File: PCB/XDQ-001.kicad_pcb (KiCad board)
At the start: 4 copper layers, 45 x 50 mm, 66 parts, among them J1 RADIO, J2 ESC, J3 GPS, J4 SWD, J5 USB_B_Micro, J6 BEC CONECTOR, U1 USBLC6-2P6, U2 AP2112K-3.3, U3 STM32F411CEUx, U4 AP2112K-3.3, U5 W25Q32JVSS, U6 AP2112K-3.3, U7 ICM-42688-P, U8 BMP280, U9 MMC5983MA, Y1 8Mhz

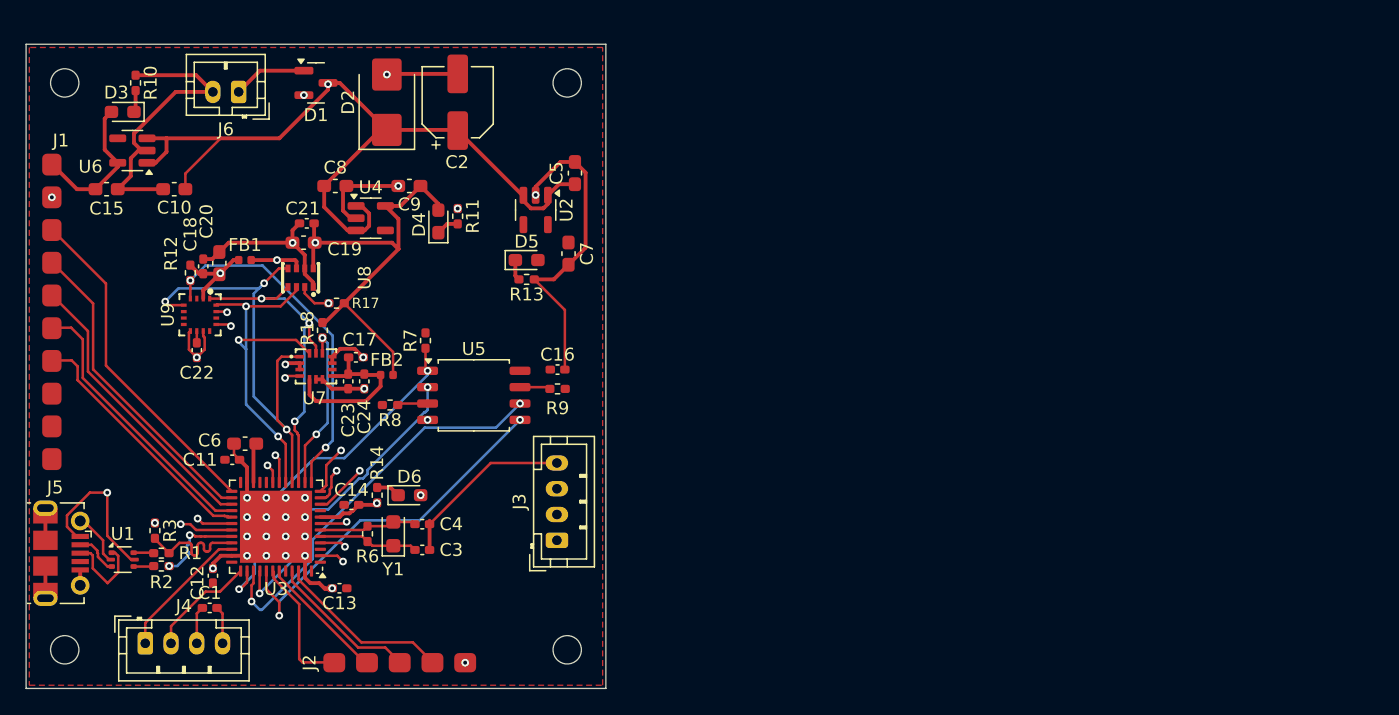
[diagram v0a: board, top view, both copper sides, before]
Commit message: Updated FCB and documentation
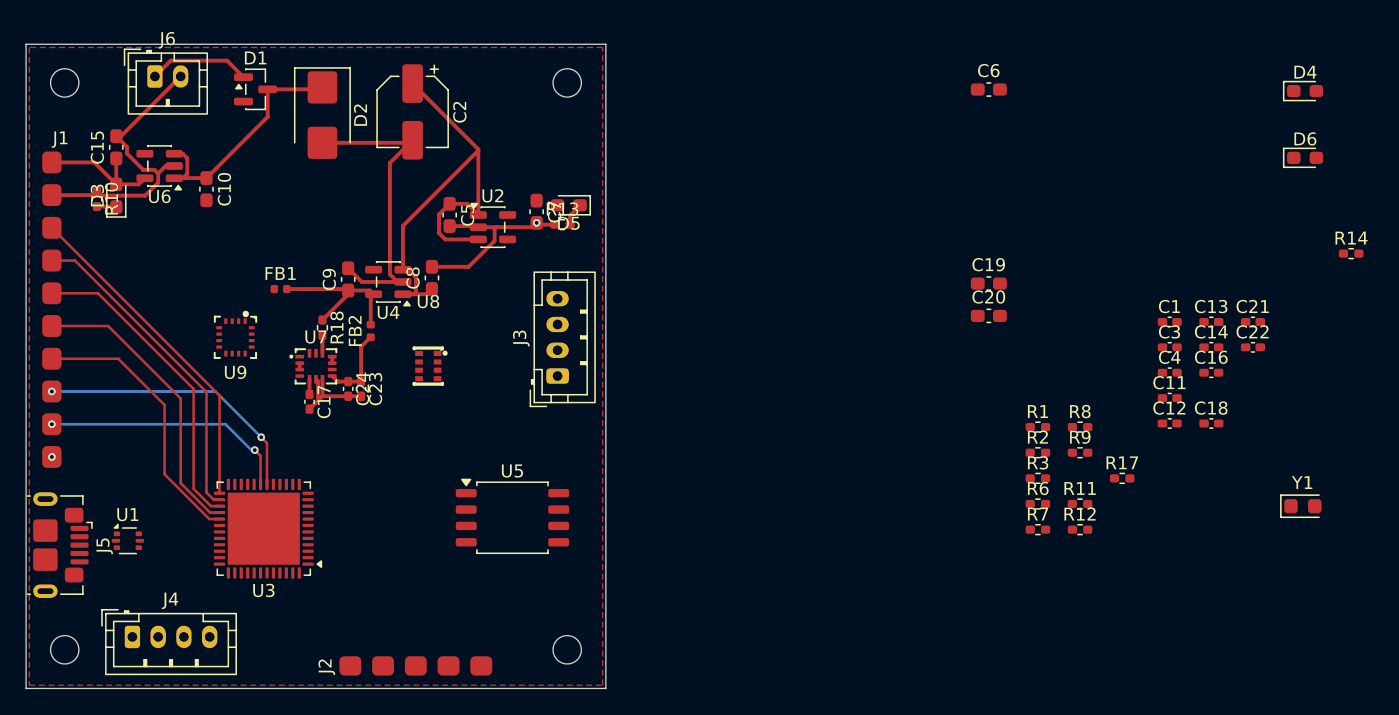
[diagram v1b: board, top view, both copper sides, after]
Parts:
- J5: footprint Connector_USB:USB_Micro-B_Molex-105017-0001 -> huellas_simplificadas:USB_Micro-B_GCT_USB3076-30-A
- moved C22 82.0 mm to (184.2, 97.5), turned to 0 degrees
- moved C18 79.2 mm to (181.0, 103.4), turned to 0 degrees
- moved R14 77.9 mm to (191.8, 90.2), turned to 0 degrees
- moved C1 77.8 mm to (177.8, 95.6)
- moved C12 75.2 mm to (177.8, 103.4), turned to 0 degrees
- moved D6 74.3 mm to (188.3, 82.8)
- moved C21 73.8 mm to (184.2, 95.6), turned to 0 degrees
- moved C11 72.9 mm to (177.8, 101.5)
- moved R12 71.9 mm to (170.8, 111.7), turned to 0 degrees
- moved C13 70.8 mm to (181.0, 95.6), turned to 0 degrees
- moved Y1 70.6 mm to (188.1, 109.9), turned to 0 degrees
- moved R1 68.7 mm to (167.5, 103.7), turned to 0 degrees
- moved R3 68.7 mm to (167.5, 107.7), turned to 0 degrees
- moved R2 68.6 mm to (167.5, 105.7), turned to 0 degrees
- moved D4 68.0 mm to (188.3, 77.6), turned to 0 degrees
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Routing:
- net GND: track 142.3 -> 70.6 mm, vias 31 -> 1
- net /VBUS: track 49.5 -> 0.00 mm, vias 2 -> 0
- net /GPS_TX: track 37.2 -> 0.00 mm, vias 1 -> 0
- net /IMU_MISO: track 36.7 -> 0.00 mm, vias 3 -> 0
- net /GPS_RX: track 34.9 -> 0.00 mm, vias 1 -> 0
- net /FLASH_SCK: track 31.0 -> 0.00 mm, vias 2 -> 0
- net +3V3_ANALOG: track 42.9 -> 12.5 mm, vias 2 -> 0
- net /FLASH_MOSI: track 29.5 -> 0.00 mm, vias 2 -> 0
- net /IMU_MOSI: track 29.0 -> 0.00 mm, vias 3 -> 0
- net /NRESET: track 28.0 -> 0.00 mm
- net /FLASH_CS: track 28.0 -> 0.00 mm, vias 2 -> 0
- net /MAG_CS: track 27.3 -> 0.00 mm, vias 2 -> 0
- net /IMU_SCK: track 26.5 -> 0.00 mm, vias 3 -> 0
- net /FLASH_MISO: track 24.6 -> 0.00 mm, vias 2 -> 0
- net /NRST: track 23.4 -> 0.00 mm, vias 1 -> 0
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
